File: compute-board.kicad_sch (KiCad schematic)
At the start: 38 parts, among them J1 PC104, J2 ESP_PROG, J3 ESP_PROGRAM, J4 i2c, J5 104031-0811, J6 RST, SW1 ESP Program, SW2 WEB_CONF, U1 ESP32-WROOM-32E, U2 XC6220B331MR, U3 TPS3839DBZ, U4 XC6220B331MR

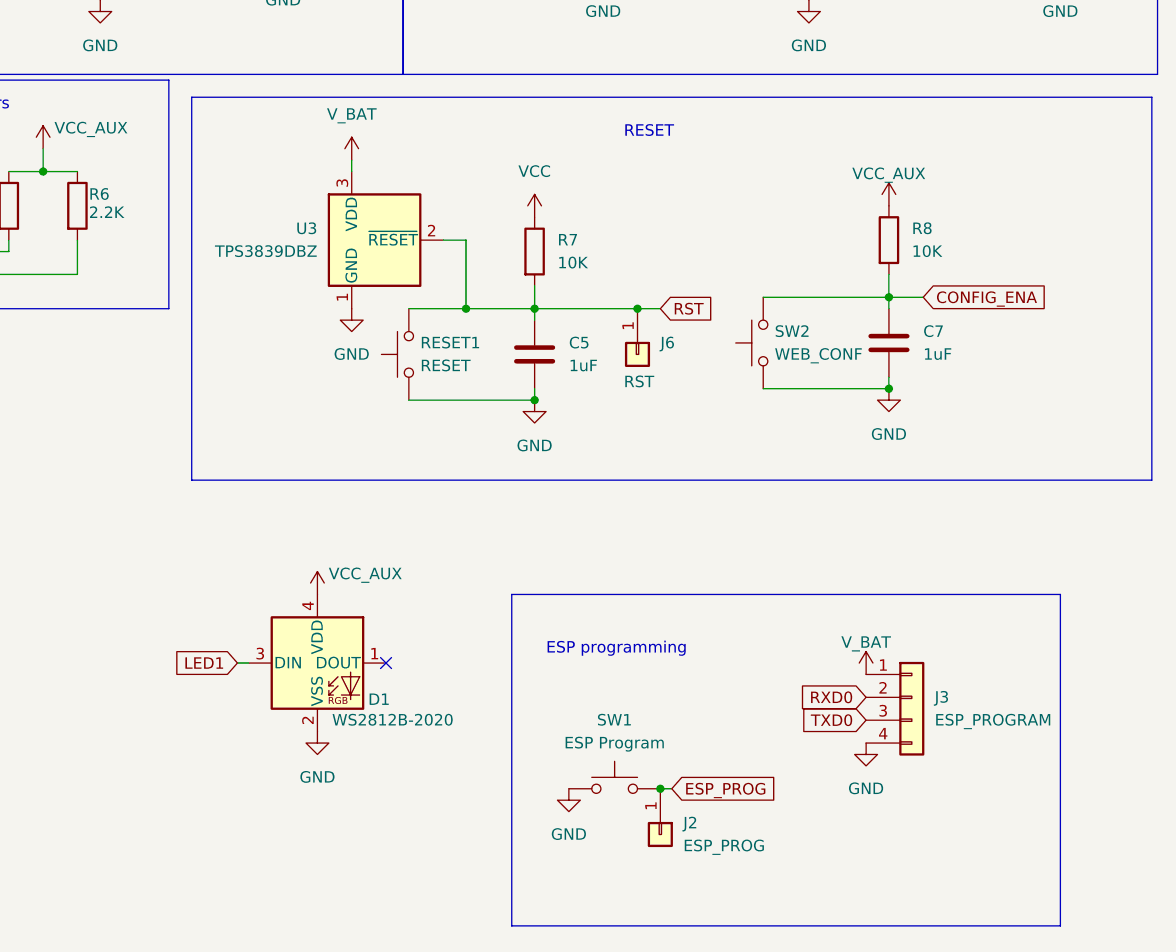
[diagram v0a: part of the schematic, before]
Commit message: (fix): various hardware designgs issues.
1. Add thermal reliefs.
2. Remove Pullup on CONFIG button, this was causing the esp32 to select
   1.8v FLASH.
3. Replace addresable led with a single color led.
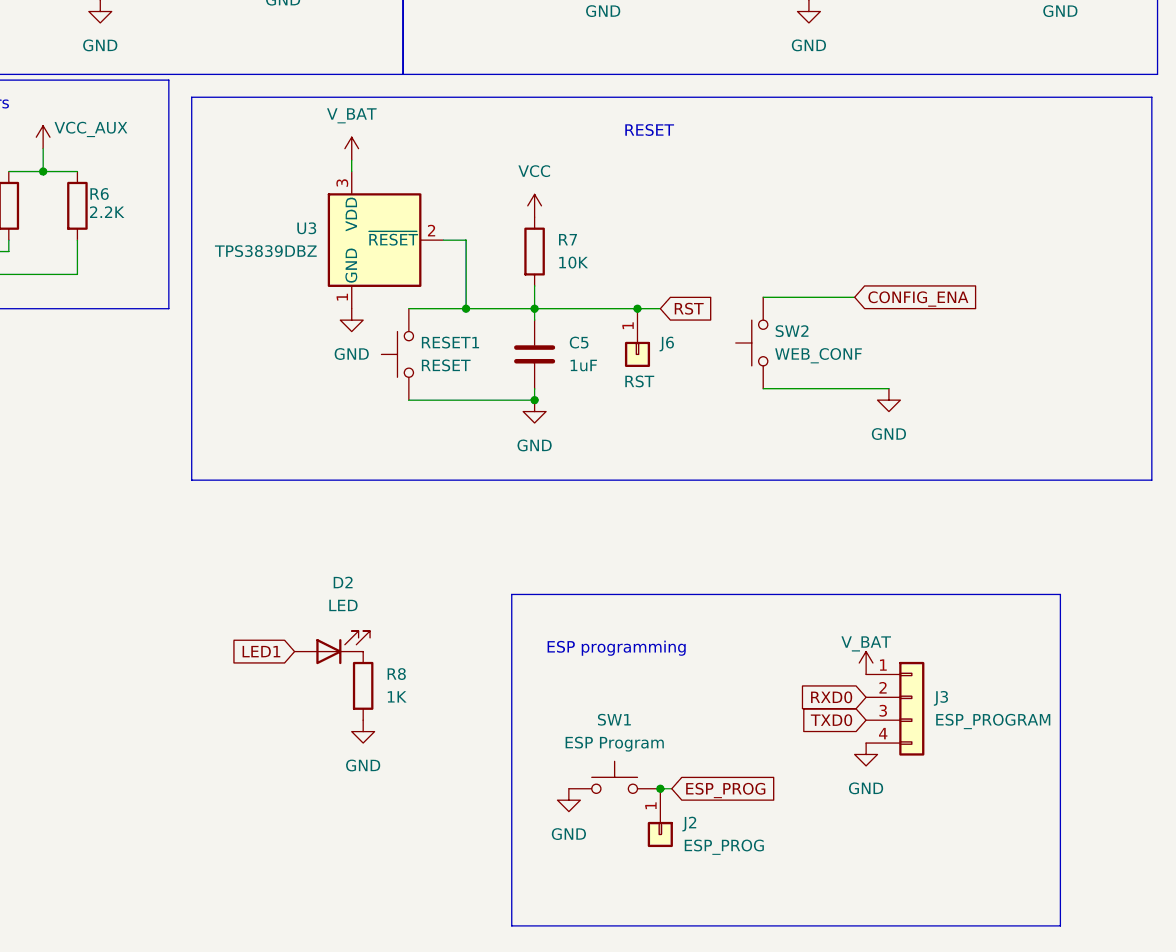
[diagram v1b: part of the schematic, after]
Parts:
- removed C7: 1uF, Capacitor_SMD:C_1206_3216Metric_Pad1.33x1.80mm_HandSolder, symbol Device:C
- removed D1: WS2812B-2020, LED_SMD:LED_WS2812B-2020_PLCC4_2.0x2.0mm, symbol LED:WS2812B-2020
- added D2: LED, LED_SMD:LED_0603_1608Metric_Pad1.05x0.95mm_HandSolder, symbol Device:LED
- R8: value 10K -> 1K
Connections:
- net CONFIG_ENA: no longer R8.2
- net GND: now also R8.2
- net LED1: now also D2.2 (A)
- net VCC_AUX: no longer R8.1
- new net: D2.1 (K), R8.1
- no-connect marks 9 -> 8
